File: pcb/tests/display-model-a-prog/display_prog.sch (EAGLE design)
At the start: 9 parts, among them J1 SNG-2MM-HEADER-07-V, J2 SNG-2MM-HEADER-07-V, J3 SNG-100-HEADER-06-FL-V, J4 TC2030-MCP, U1 LM431BCM3

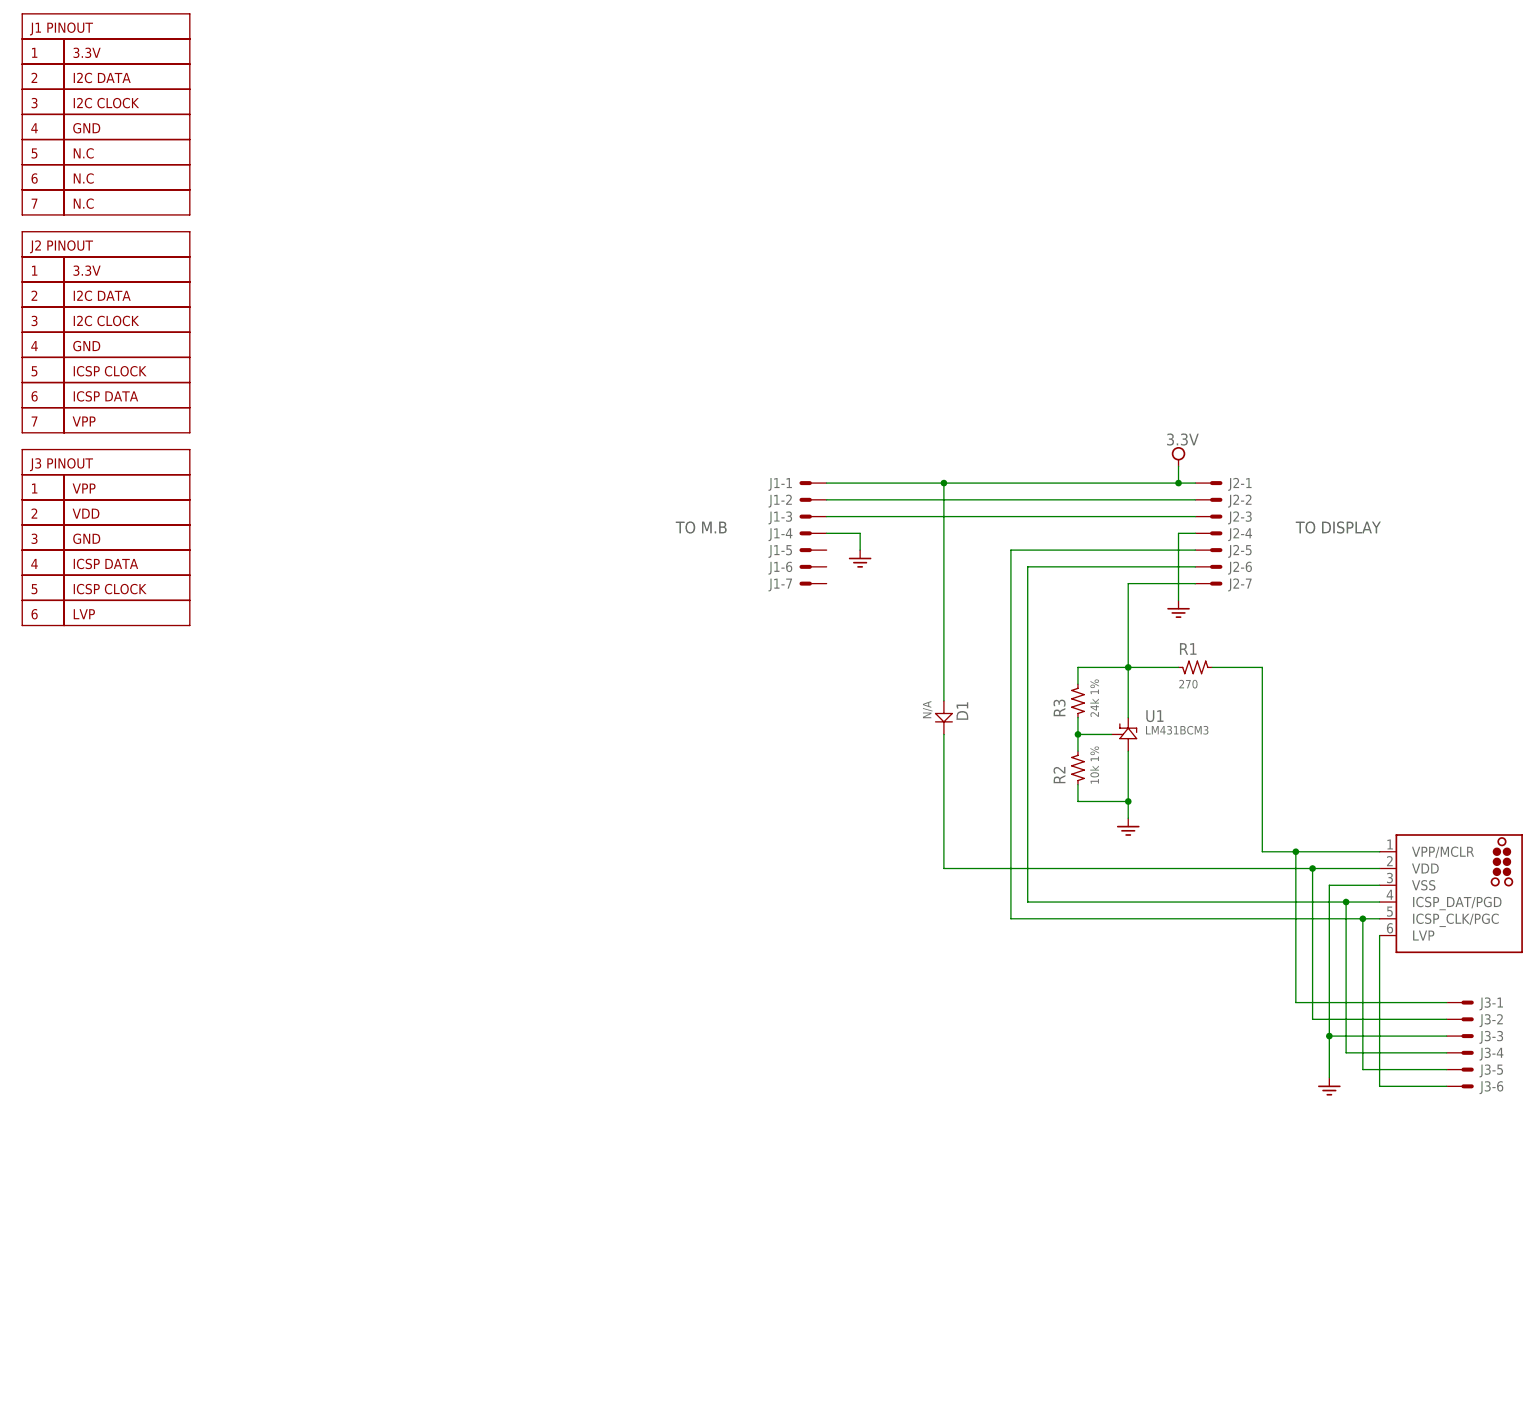
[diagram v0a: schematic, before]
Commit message: Changed page format on schematics to US letter (8.5" x 11")
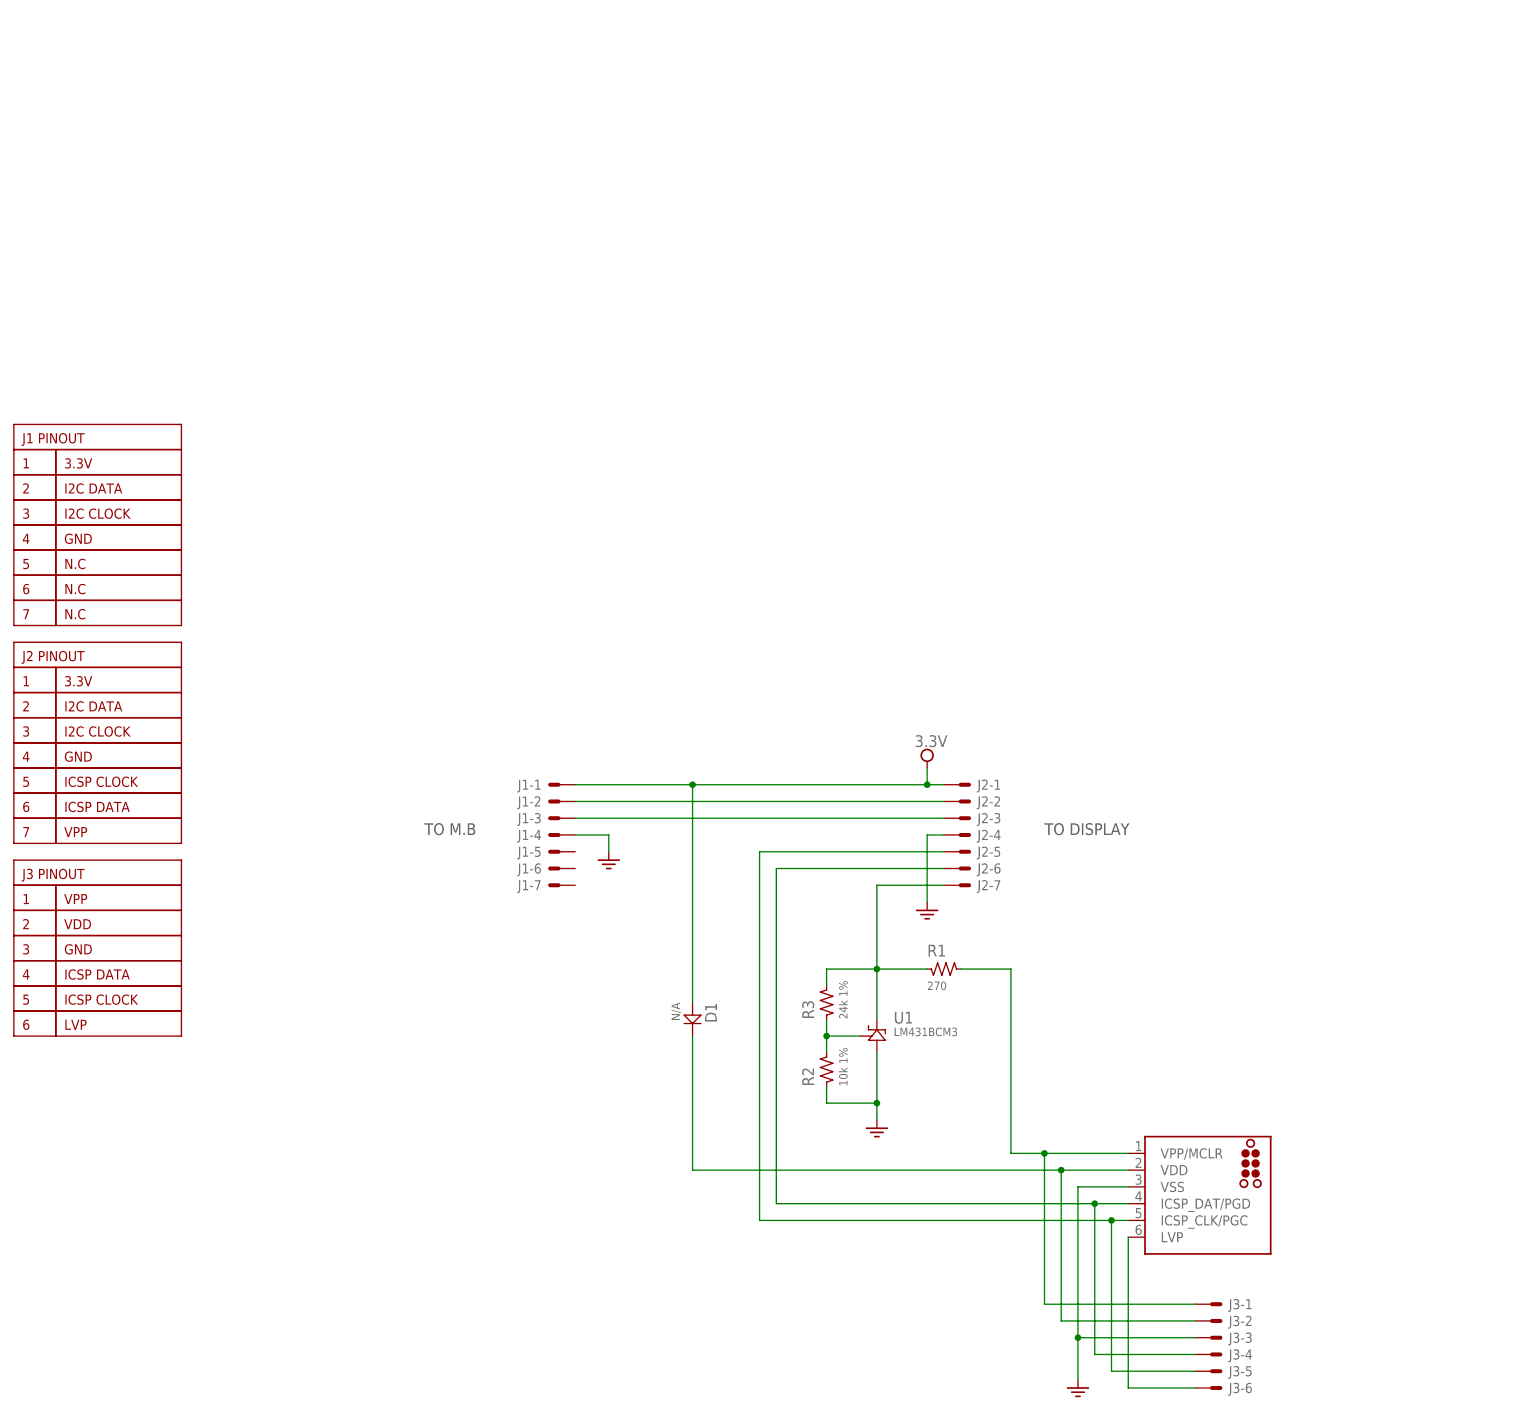
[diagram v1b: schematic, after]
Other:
- moved on the sheet: D1, J1-1, J1-2, J1-3, J1-4, J1-5, J1-6, J1-7, J2-1, J2-2, J2-3, J2-4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
